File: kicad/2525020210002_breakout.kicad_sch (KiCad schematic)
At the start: 13 parts, among them J1 JST_PH_B4B-PH-K, J2 JST_PH_B4B-PH-K, J3 Conn_01x04_Socket, U1 2525020210002

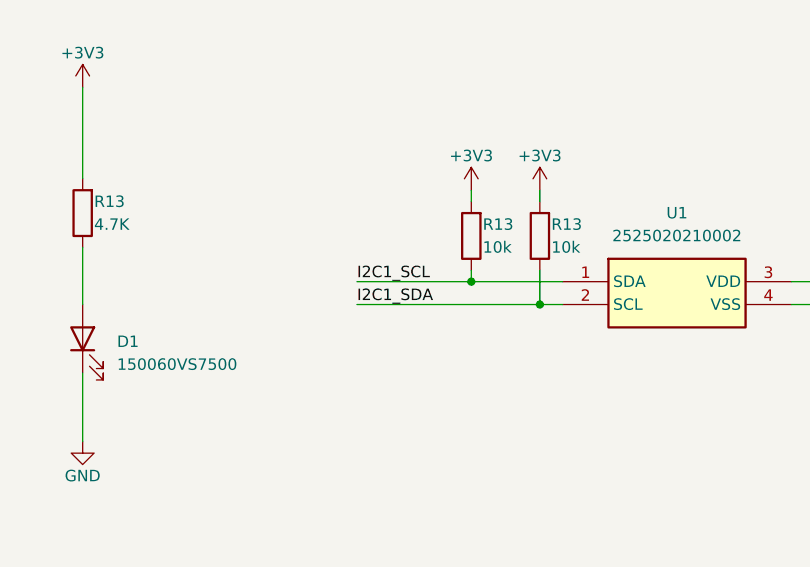
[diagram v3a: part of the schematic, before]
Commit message: Swapped SDA & SCL pins, rounded edgecuts
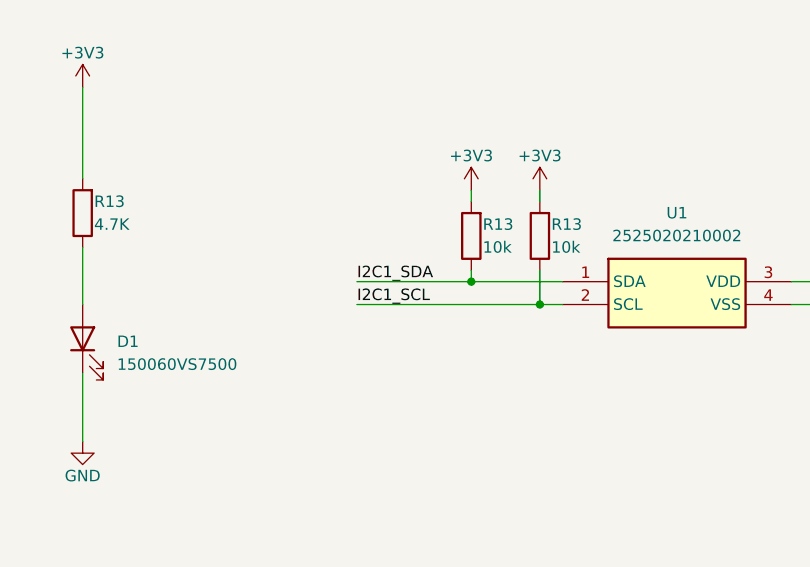
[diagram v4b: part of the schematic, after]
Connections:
- net I2C1_SCL: now also U1.2 (SCL); no longer U1.1 (SDA)
- net I2C1_SDA: now also U1.1 (SDA); no longer U1.2 (SCL)
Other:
- moved on the sheet: R13
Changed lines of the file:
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@@
     (effects (font (size 1.27 1.27)) (justify right bottom))
   )
-  (label "I2C1_SDA" (at 124.46 96.52 0) (fields_autoplaced)
+  (label "I2C1_SDA" (at 124.46 93.98 0) (fields_autoplaced)
     (effects (font (size 1.27 1.27)) (justify left bottom))
   )
@@
     (effects (font (size 1.27 1.27)) (justify right bottom))
   )
-  (label "I2C1_SCL" (at 124.46 93.98 0) (fields_autoplaced)
+  (label "I2C1_SCL" (at 124.46 96.52 0) (fields_autoplaced)
     (effects (font (size 1.27 1.27)) (justify left bottom))
   )
@@
     (effects (font (size 1.27 1.27)) (justify left bottom))
   )
-  (symbol (lib_id "Device:R") (at 137.16 88.9 180) (unit 1)
-    (in_bom yes) (on_board yes) (dnp no)
-    (property "Reference" "R13" (at 138.43 87.63 0)
-      (effects (font (size 1.27 1.27)) (justify right))
-    )
-    (property "Value" "10k" (at 138.43 90.17 0)
-      (effects (font (size 1.27 1.27)) (justify right))
-    )
-    (property "Footprint" "Resistor_SMD:R_0603_1608Metric" (at 138.938 88.9 90)
-      (effects (font (size 1.27 1.27)) hide)
-    )
-    (property "Datasheet" "~" (at 137.16 88.9 0)
+  (symbol (lib_id "Device:R") (at 144.78 88.9 180) (unit 1)
+    (in_bom yes) (on_board yes) (dnp no)
+    (property "Reference" "R13" (at 146.05 87.63 0)
+      (effects (font (size 1.27 1.27)) (justify right))
+    )
+    (property "Value" "10k" (at 146.05 90.17 0)
+      (effects (font (size 1.27 1.27)) (justify right))
+    )
+    (property "Footprint" "Resistor_SMD:R_0603_1608Metric" (at 146.558 88.9 90)
+      (effects (font (size 1.27 1.27)) hide)
+    )
+    (property "Datasheet" "~" (at 144.78 88.9 0)
       (effects (font (size 1.27 1.27)) hide)
     )
@@
     )
   )
-  (symbol (lib_id "Device:R") (at 144.78 88.9 180) (unit 1)
-    (in_bom yes) (on_board yes) (dnp no)
-    (property "Reference" "R13" (at 146.05 87.63 0)
-      (effects (font (size 1.27 1.27)) (justify right))
-    )
-    (property "Value" "10k" (at 146.05 90.17 0)
-      (effects (font (size 1.27 1.27)) (justify right))
-    )
-    (property "Footprint" "Resistor_SMD:R_0603_1608Metric" (at 146.558 88.9 90)
-      (effects (font (size 1.27 1.27)) hide)
-    )
-    (property "Datasheet" "~" (at 144.78 88.9 0)
-      (effects (font (size 1.27 1.27)) hide)
-    )
+  (symbol (lib_id "Device:R") (at 137.16 88.9 180) (unit 1)
+    (in_bom yes) (on_board yes) (dnp no)
+    (property "Reference" "R13" (at 138.43 87.63 0)
+      (effects (font (size 1.27 1.27)) (justify right))
+    )
+    (property "Value" "10k" (at 138.43 90.17 0)
+      (effects (font (size 1.27 1.27)) (justify right))
+    )
+    (property "Footprint" "Resistor_SMD:R_0603_1608Metric" (at 138.938 88.9 90)
+      (effects (font (size 1.27 1.27)) hide)
+    )
+    (property "Datasheet" "~" (at 137.16 88.9 0)
+      (effects (font (size 1.27 1.27)) hide)
+    )
